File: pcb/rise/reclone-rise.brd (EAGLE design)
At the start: 85 x 56 mm, 130 parts, among them Y1 12MHz

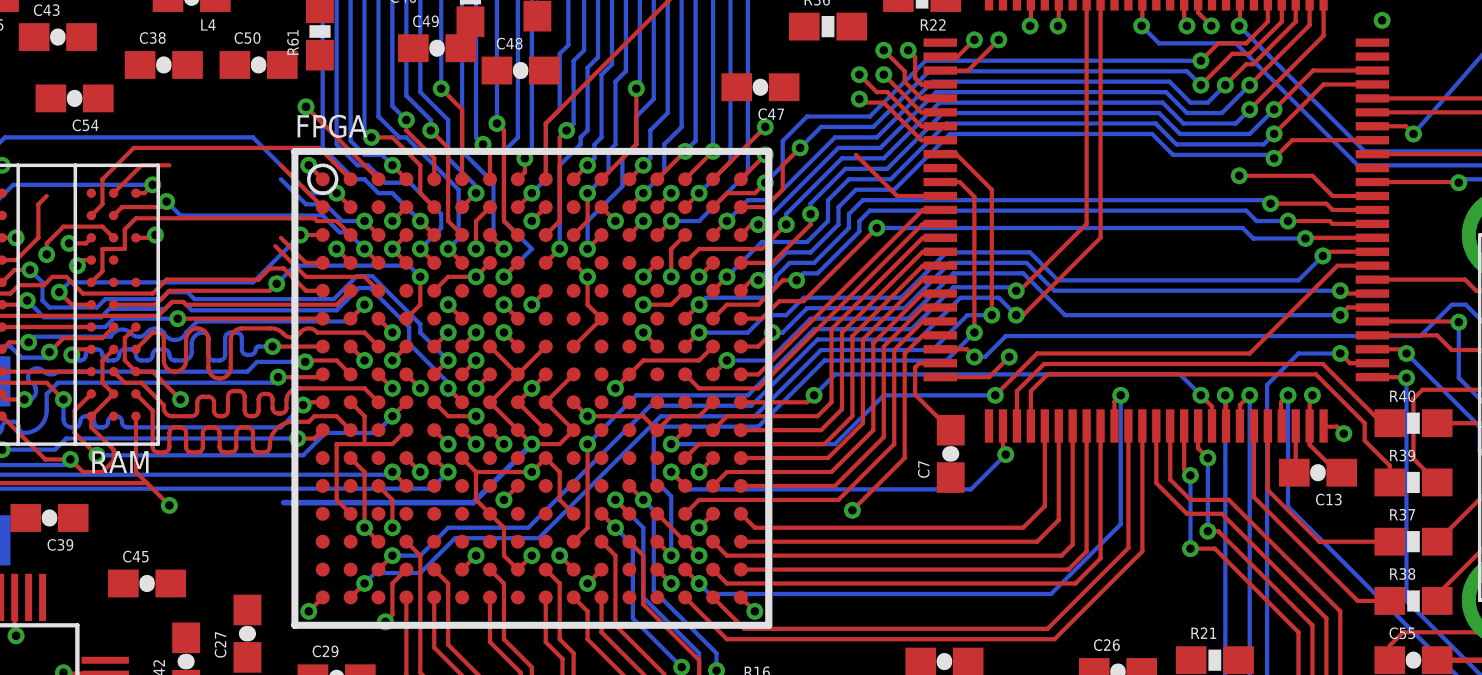
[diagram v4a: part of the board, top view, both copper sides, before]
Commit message: Only 8 DDR2 traces left
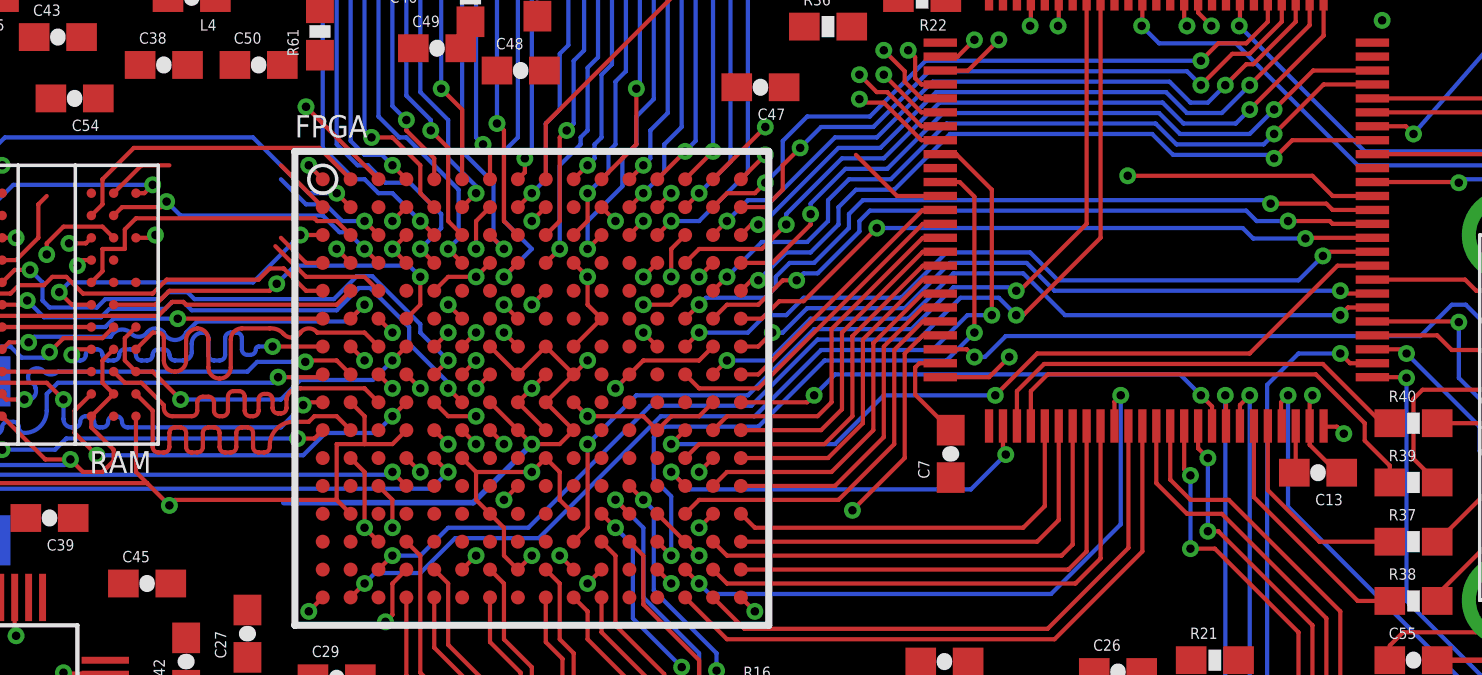
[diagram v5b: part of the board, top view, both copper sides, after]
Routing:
- net +1V2: track 23.8 -> 50.7 mm, vias 1 -> 2
- net +1V8: track 97.1 -> 107.7 mm
- net JTAG_TMS: track 119.6 -> 120.2 mm
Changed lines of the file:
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@@
 <wire x1="33.5" y1="38.5" x2="33.25" y2="38.75" width="0.1524" layer="1"/>
 <wire x1="33.25" y1="38.75" x2="33" y2="39" width="0.1524" layer="16"/>
-<wire x1="33" y1="39" x2="33" y2="47" width="0.1524" layer="16"/>
 <wire x1="33" y1="47" x2="30" y2="50" width="0.1524" layer="16"/>
 <wire x1="30" y1="50" x2="30" y2="52.46" width="0.1524" layer="16"/>
 <wire x1="30" y1="52.46" x2="28.69" y2="53.77" width="0.1524" layer="16"/>
+<wire x1="33" y1="39" x2="33" y2="47" width="0.1524" layer="16"/>
 </signal>
 <signal name="GPIO13">
@@
 <via x="30" y="31" extent="1-16" drill="0.3048" shape="octagon"/>
 <wire x1="30.5" y1="31.5" x2="30" y2="31" width="0.1524" layer="1"/>
-<wire x1="28.5" y1="25.5" x2="28" y2="26" width="0.1524" layer="1"/>
-<wire x1="28" y1="26" x2="28" y2="28" width="0.1524" layer="1"/>
 <wire x1="28" y1="28" x2="29" y2="28" width="0.1524" layer="1"/>
 <wire x1="29" y1="28" x2="29" y2="29" width="0.1524" layer="1"/>
@@
 <wire x1="30" y1="28" x2="29" y2="28" width="0.1524" layer="1"/>
 <via x="28" y="35" extent="1-16" drill="0.3048" shape="octagon"/>
-<wire x1="28.5" y1="34.5" x2="28" y2="35" width="0.1524" layer="1"/>
-<wire x1="28" y1="35" x2="28" y2="36.2" width="0.1524" layer="15"/>
-<wire x1="28" y1="36.2" x2="26.1" y2="38.1" width="0.1524" layer="15"/>
-<wire x1="30" y1="31" x2="29" y2="32" width="0.1524" layer="15"/>
-<wire x1="29" y1="32" x2="28.6" y2="32" width="0.1524" layer="15"/>
-<wire x1="28.6" y1="32" x2="28.2" y2="32.4" width="0.1524" layer="15"/>
-<wire x1="28.2" y1="32.4" x2="25.4" y2="32.4" width="0.1524" layer="15"/>
-<wire x1="25.4" y1="32.4" x2="23.9" y2="33.9" width="0.1524" layer="15"/>
 <contactref element="R61" pad="2"/>
 <contactref element="RAM" pad="L1"/>
@@
 <wire x1="16.4" y1="37.3" x2="13.7" y2="34.6" width="0.1524" layer="16"/>
 <wire x1="20.8" y1="37" x2="21.1" y2="37" width="0.1524" layer="1"/>
-<wire x1="21.1" y1="37" x2="21.4" y2="37.3" width="0.1524" layer="1"/>
 <wire x1="13.7" y1="34.6" x2="12.5" y2="33.4" width="0.1524" layer="1"/>
 <wire x1="13.7" y1="34.6" x2="14.4" y2="34.6" width="0.1524" layer="1"/>
@@
 <wire x1="21.4" y1="30.6" x2="22.4" y2="29.6" width="0.1524" layer="1"/>
 <wire x1="20.4" y1="31" x2="20.8" y2="30.6" width="0.1524" layer="1"/>
+<wire x1="30" y1="31" x2="29.3" y2="30.3" width="0.1524" layer="16"/>
+<wire x1="29.3" y1="30.3" x2="26.7" y2="30.3" width="0.1524" layer="16"/>
+<wire x1="26.7" y1="30.3" x2="26" y2="29.6" width="0.1524" layer="16"/>
+<wire x1="26" y1="29.6" x2="22.4" y2="29.6" width="0.1524" layer="16"/>
+<wire x1="28" y1="26" x2="22.2" y2="26" width="0.1524" layer="1"/>
+<wire x1="22.2" y1="26" x2="22" y2="25.8" width="0.1524" layer="1"/>
+<wire x1="28" y1="26" x2="28" y2="28" width="0.1524" layer="1"/>
+<wire x1="28.5" y1="25.5" x2="28" y2="26" width="0.1524" layer="1"/>
+<wire x1="28" y1="35" x2="25.7" y2="37.3" width="0.1524" layer="15"/>
+<wire x1="28.5" y1="34.5" x2="28" y2="35" width="0.1524" layer="1"/>
+<wire x1="21.4" y1="37.3" x2="25.7" y2="37.3" width="0.1524" layer="15"/>
+<wire x1="21.1" y1="37" x2="21.4" y2="37.3" width="0.1524" layer="1"/>
 <wire x1="22.65" y1="41.6" x2="27.4" y2="43.65" width="0" layer="19" extent="1-1"/>
 <wire x1="18.85" y1="42.6" x2="22.65" y2="41.6" width="0" layer="19" extent="1-1"/>
@@
 <wire x1="13.35" y1="25.6" x2="14.4" y2="28.1" width="0" layer="19" extent="1-1"/>
 <wire x1="15.4501" y1="22.5001" x2="16.85" y2="25.35" width="0" layer="19" extent="1-1"/>
-<wire x1="23.9" y1="33.9" x2="20.8" y2="32.2" width="0" layer="19" extent="1-15"/>
-<wire x1="28.5" y1="34.5" x2="28.2" y2="32.4" width="0" layer="19" extent="1-15"/>
-<wire x1="28.5" y1="29.5" x2="30" y2="31" width="0" layer="19" extent="1-1"/>
 <wire x1="22.6" y1="21.05" x2="22" y2="25.8" width="0" layer="19" extent="1-15"/>
 </signal>
@@
 <wire x1="41.5" y1="37.5" x2="43.375" y2="39.375" width="0.1524" layer="1"/>
 <wire x1="43.375" y1="39.375" x2="59.625" y2="39.375" width="0.1524" layer="15"/>
-<wire x1="59.625" y1="39.375" x2="67" y2="32" width="0.1524" layer="15"/>
-<wire x1="67" y1="32" x2="67" y2="30" width="0.1524" layer="15"/>
-<wire x1="67" y1="30" x2="66" y2="29.125" width="0.1524" layer="15"/>
-<wire x1="66" y1="29.125" x2="62.75" y2="29.125" width="0.1524" layer="15"/>
+<wire x1="59.625" y1="39.375" x2="67.4" y2="31.6" width="0.1524" layer="15"/>
+<wire x1="67.4" y1="31.6" x2="67.4" y2="30.1" width="0.1524" layer="15"/>
+<wire x1="67.4" y1="30.1" x2="66.4" y2="29.125" width="0.1524" layer="15"/>
+<wire x1="66.4" y1="29.125" x2="62.75" y2="29.125" width="0.1524" layer="15"/>
 <wire x1="62.75" y1="29.125" x2="62.125" y2="29.75" width="0.1524" layer="15"/>
 <via x="22.25" y="13.25" extent="1-16" drill="0.3048" shape="octagon"/>
@@
 <via x="39" y="36" extent="1-16" drill="0.3048" shape="octagon"/>
 <wire x1="48.625" y1="35.125" x2="51.125" y2="37.625" width="0.1524" layer="15"/>
-<via x="60.375" y="37.625" extent="1-16" drill="0.3048" shape="octagon"/>
+<via x="56.375" y="37.625" extent="1-16" drill="0.3048" shape="octagon"/>
 <wire x1="65.15" y1="36.9" x2="63.725" y2="36.9" width="0.1524" layer="1"/>
 <wire x1="63.725" y1="36.9" x2="63" y2="37.625" width="0.1524" layer="1"/>
-<wire x1="63" y1="37.625" x2="60.375" y2="37.625" width="0.1524" layer="1"/>
-<wire x1="60.375" y1="37.625" x2="51.125" y2="37.625" width="0.1524" layer="15"/>
+<wire x1="63" y1="37.625" x2="56.375" y2="37.625" width="0.1524" layer="1"/>
+<wire x1="56.375" y1="37.625" x2="51.125" y2="37.625" width="0.1524" layer="15"/>
 <wire x1="38.5" y1="35.5" x2="39" y2="36" width="0.1524" layer="1"/>
 <wire x1="39" y1="36" x2="39.875" y2="35.125" width="0.1524" layer="15"/>
@@
 <wire x1="34.5" y1="28.5" x2="33.5" y2="29.5" width="0.1524" layer="1"/>
 <wire x1="36.5" y1="28.5" x2="35.5" y2="29.5" width="0.1524" layer="1"/>
-<wire x1="35.5" y1="29.5" x2="36.5" y2="30.5" width="0.1524" layer="1"/>
 <wire x1="35.5" y1="31.5" x2="34.5" y2="30.5" width="0.1524" layer="1"/>
-<wire x1="33.5" y1="29.5" x2="34.5" y2="30.5" width="0.1524" layer="1"/>
 <wire x1="33.5" y1="31.5" x2="34.5" y2="30.5" width="0.1524" layer="1"/>
 <via x="35" y="28" extent="1-16" drill="0.3048" shape="octagon"/>
@@
 <wire x1="32.9" y1="25.9" x2="26.1" y2="25.9" width="0.2" layer="16"/>
 <wire x1="34.5" y1="28.5" x2="35" y2="28" width="0.1524" layer="1"/>
+<via x="37" y="31" extent="1-16" drill="0.3048" shape="octagon"/>
+<wire x1="35.5" y1="29.5" x2="36.5" y2="30.5" width="0.1524" layer="1"/>
+<wire x1="37" y1="31" x2="37.7" y2="31.7" width="0.3048" layer="15"/>
+<wire x1="37.7" y1="31.7" x2="37.7" y2="35.3" width="0.3048" layer="15"/>
+<wire x1="37.7" y1="35.3" x2="35.5" y2="37.5" width="0.3048" layer="15"/>
+<wire x1="35.5" y1="37.5" x2="35.5" y2="42.4" width="0.3048" layer="15"/>
+<wire x1="37" y1="31" x2="36.3" y2="30.3" width="0.3048" layer="15"/>
+<wire x1="36.3" y1="30.3" x2="36.3" y2="26.6" width="0.3048" layer="15"/>
+<wire x1="36.3" y1="26.6" x2="34.3" y2="24.6" width="0.3048" layer="15"/>
+<wire x1="34.3" y1="24.6" x2="34.3" y2="23.6" width="0.3048" layer="15"/>
+<wire x1="34.3" y1="23.6" x2="37.3" y2="20.6" width="0.3048" layer="15"/>
+<wire x1="37.3" y1="20.6" x2="37.3" y2="19.8" width="0.3048" layer="15"/>
+<wire x1="36.5" y1="30.5" x2="37" y2="31" width="0.1524" layer="1"/>
+<wire x1="35.5" y1="31.5" x2="36.5" y2="30.5" width="0.1524" layer="1"/>
 <wire x1="35.45" y1="41.4" x2="42.35" y2="40.8" width="0" layer="19" extent="1-1"/>
-<wire x1="32.45" y1="42.2" x2="35.45" y2="41.4" width="0" layer="19" extent="1-1"/>
+<wire x1="35.5" y1="42.4" x2="35.45" y2="41.4" width="0" layer="19" extent="1-15"/>
+<wire x1="32.45" y1="42.2" x2="35.5" y2="42.4" width="0" layer="19" extent="1-15"/>
 <wire x1="29.15" y1="45" x2="32.45" y2="42.2" width="0" layer="19" extent="1-1"/>
 <wire x1="26.05" y1="41.6" x2="29.15" y2="45" width="0" layer="19" extent="1-1"/>
 <wire x1="21.95" y1="44" x2="26.05" y2="41.6" width="0" layer="19" extent="1-1"/>
-<wire x1="35.5" y1="31.5" x2="35.45" y2="41.4" width="0" layer="19" extent="1-1"/>
 <wire x1="22.05" y1="23" x2="26.1" y2="25.9" width="0" layer="19" extent="1-16"/>
 </signal>

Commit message: Finished routing DDR2 and FPGA traces!
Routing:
- net M3A11: track 4.36 -> 15.5 mm, vias 0 -> 2
- net M3A4: track 10.4 -> 21.5 mm, vias 2 -> 3
- net M3A2: track 5.13 -> 15.9 mm, vias 0 -> 2
- net M3BA0: track 4.33 -> 11.8 mm, vias 1 -> 3
- net M3A10: track 11.0 -> 18.0 mm, vias 1 -> 3
- net M3BA2: track 2.12 -> 8.18 mm, vias 0 -> 2
- net M3A12: track 9.65 -> 15.5 mm, vias 1 -> 2
- net M3A13: track 16.0 -> 21.4 mm
- net M3A7: track 10.6 -> 7.34 mm
- net M3A9: track 11.3 -> 12.1 mm

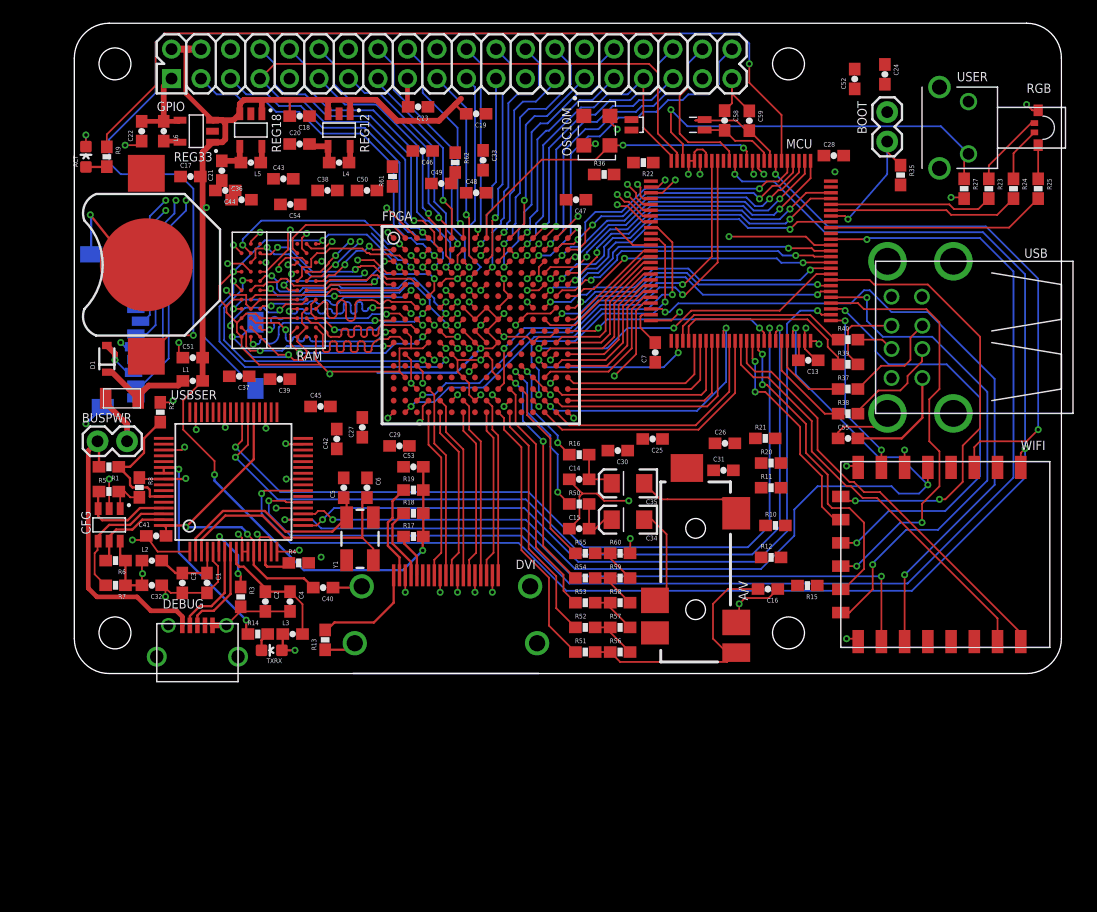
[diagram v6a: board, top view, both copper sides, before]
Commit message: Routed JTAG pull up/down resistors
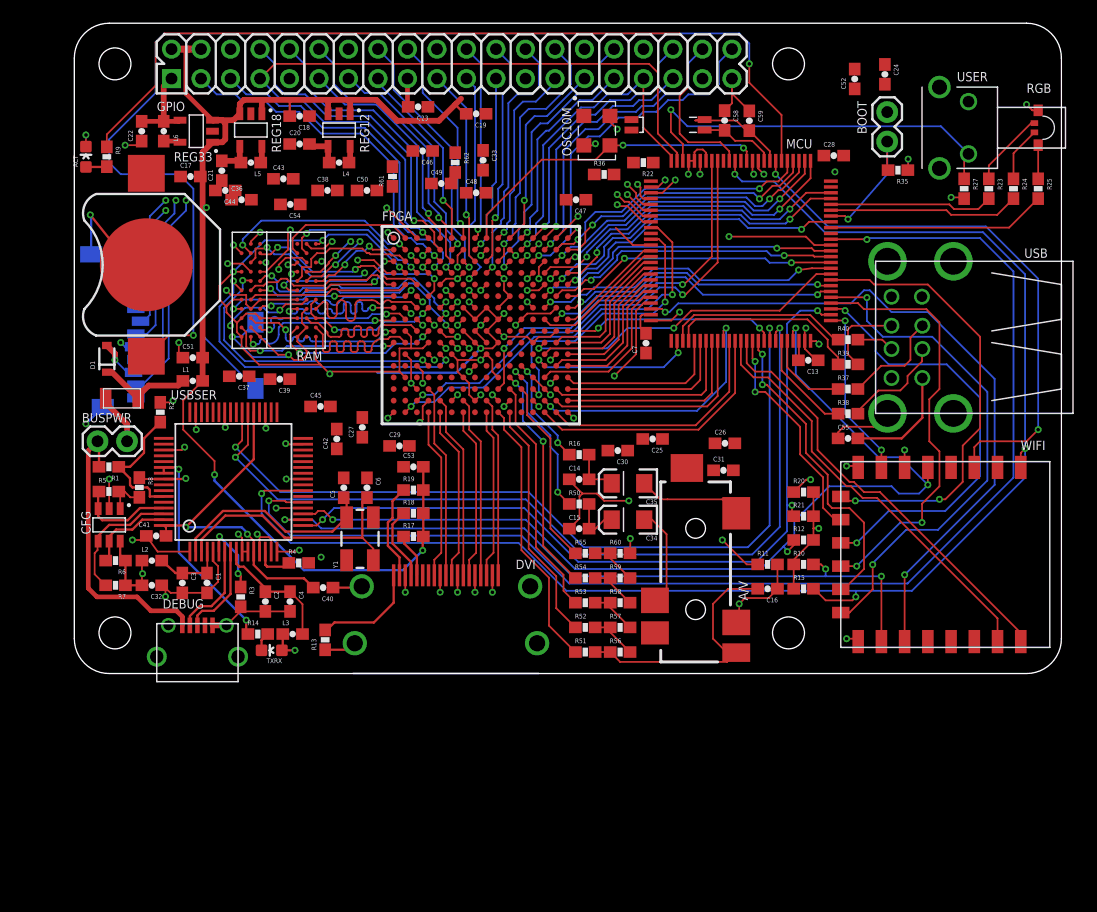
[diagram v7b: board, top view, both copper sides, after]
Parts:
- moved R21 7.47 mm to (62.8, 13.6)
- moved R11 6.61 mm to (59.7, 9.40)
- moved R10 4.14 mm to (62.8, 9.40)
- moved R20 3.75 mm to (62.8, 15.6)
- moved R12 3.18 mm to (62.8, 11.5)
- moved C7 1.13 mm to (49.2, 28.4)
- moved R35 0.48 mm to (70.9, 43.4), turned to 180 degrees
- moved R15 0.43 mm to (62.8, 7.30), turned to 0 degrees
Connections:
- removed net M3A14: FPGA.F5
- removed net M3A15: FPGA.B3
- net +3V3: now also R21.2, R35.1; no longer R21.1, R35.2
- net BOOT0: now also R35.2; no longer R35.1
- net JTAG_MCU_TDI: now also R21.1; no longer R21.2
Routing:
- net +3V3: track 77.2 -> 87.6 mm, vias 32 -> 34
- net JTAG_FPGA_TDO: track 43.6 -> 51.9 mm, vias 2 -> 3
- net JTAG_TCK: track 106.5 -> 112.9 mm, vias 4 -> 5
- net M3A7: track 7.34 -> 13.2 mm
- net /RESET: track 127.0 -> 131.7 mm, vias 3 -> 4
- net GND: track 168.4 -> 170.5 mm
- net JTAG_ESP_TDO: track 60.6 -> 62.4 mm, vias 2 -> 3
- net JTAG_MCU_TDI: track 67.6 -> 69.1 mm, vias 2 -> 3
- net JTAG_TMS: track 120.2 -> 121.4 mm, vias 4 -> 5
- net VCAP_1: track 3.74 -> 2.61 mm

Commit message: Added meanders to match lengths on differential pairs
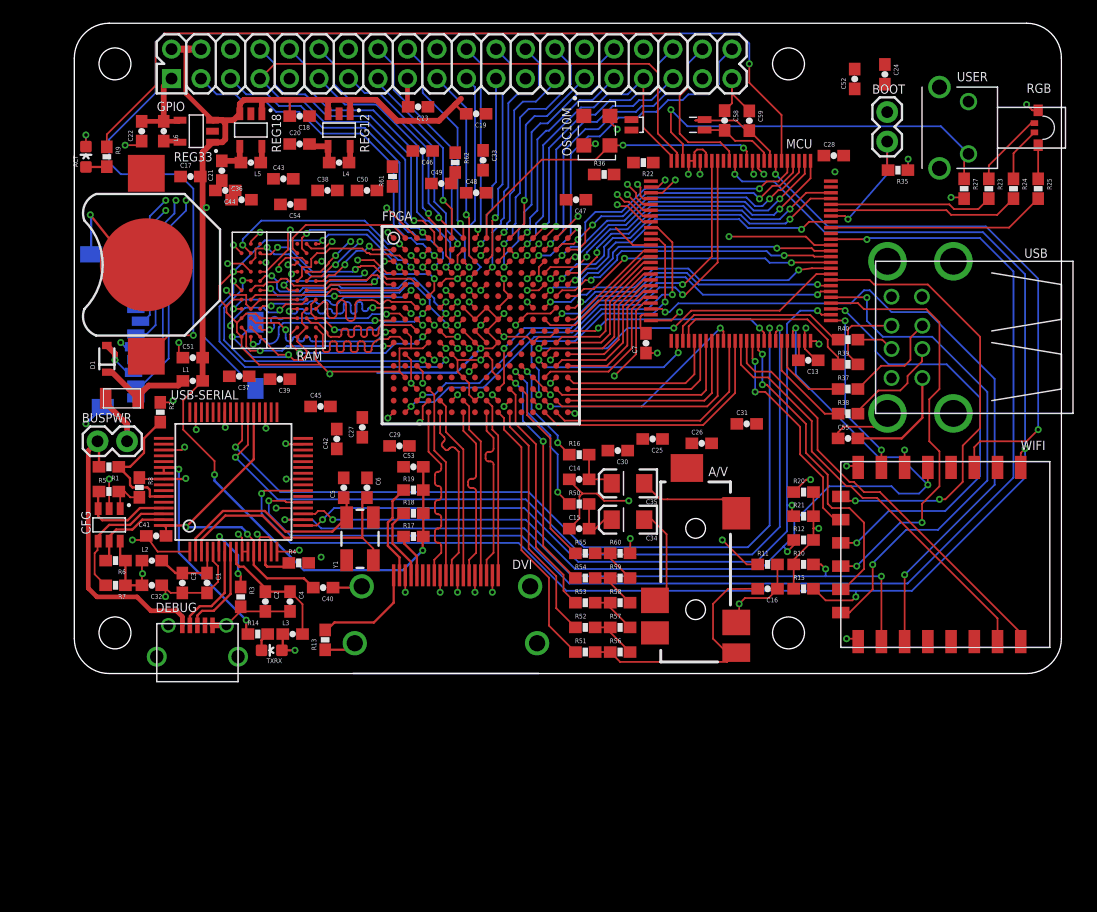
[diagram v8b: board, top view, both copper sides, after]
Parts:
- moved C31 4.47 mm to (57.9, 21.5)
- moved C26 2.00 mm to (54.0, 19.8)
- renumbered USBSER to USB-SERIAL
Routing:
- net FSMC_A18: track 22.8 -> 19.3 mm
- net FPGA_CONFIG_CLK: track 22.3 -> 19.2 mm
- net TMDS_CLKN: track 14.7 -> 16.2 mm
- net GND: track 170.5 -> 171.4 mm, vias 58 -> 59
- net TMDS_D1N: track 14.7 -> 15.5 mm
- net TMDS_D0N: track 15.0 -> 15.7 mm
- net TMDS_D2N: track 14.5 -> 15.3 mm
